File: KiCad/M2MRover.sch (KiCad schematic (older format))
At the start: 11 parts, among them J1 Light Detection, J10 MPU6050 Gyro & Acc GY-521, J2 Serial (Bluetooth), J3 Servo, J4 H-Bridge, J5 Ultrasonic Down, J6 Ultrasonic Forward, J7 Compass GY-273, J8 Left Hall, J9 Right Hall

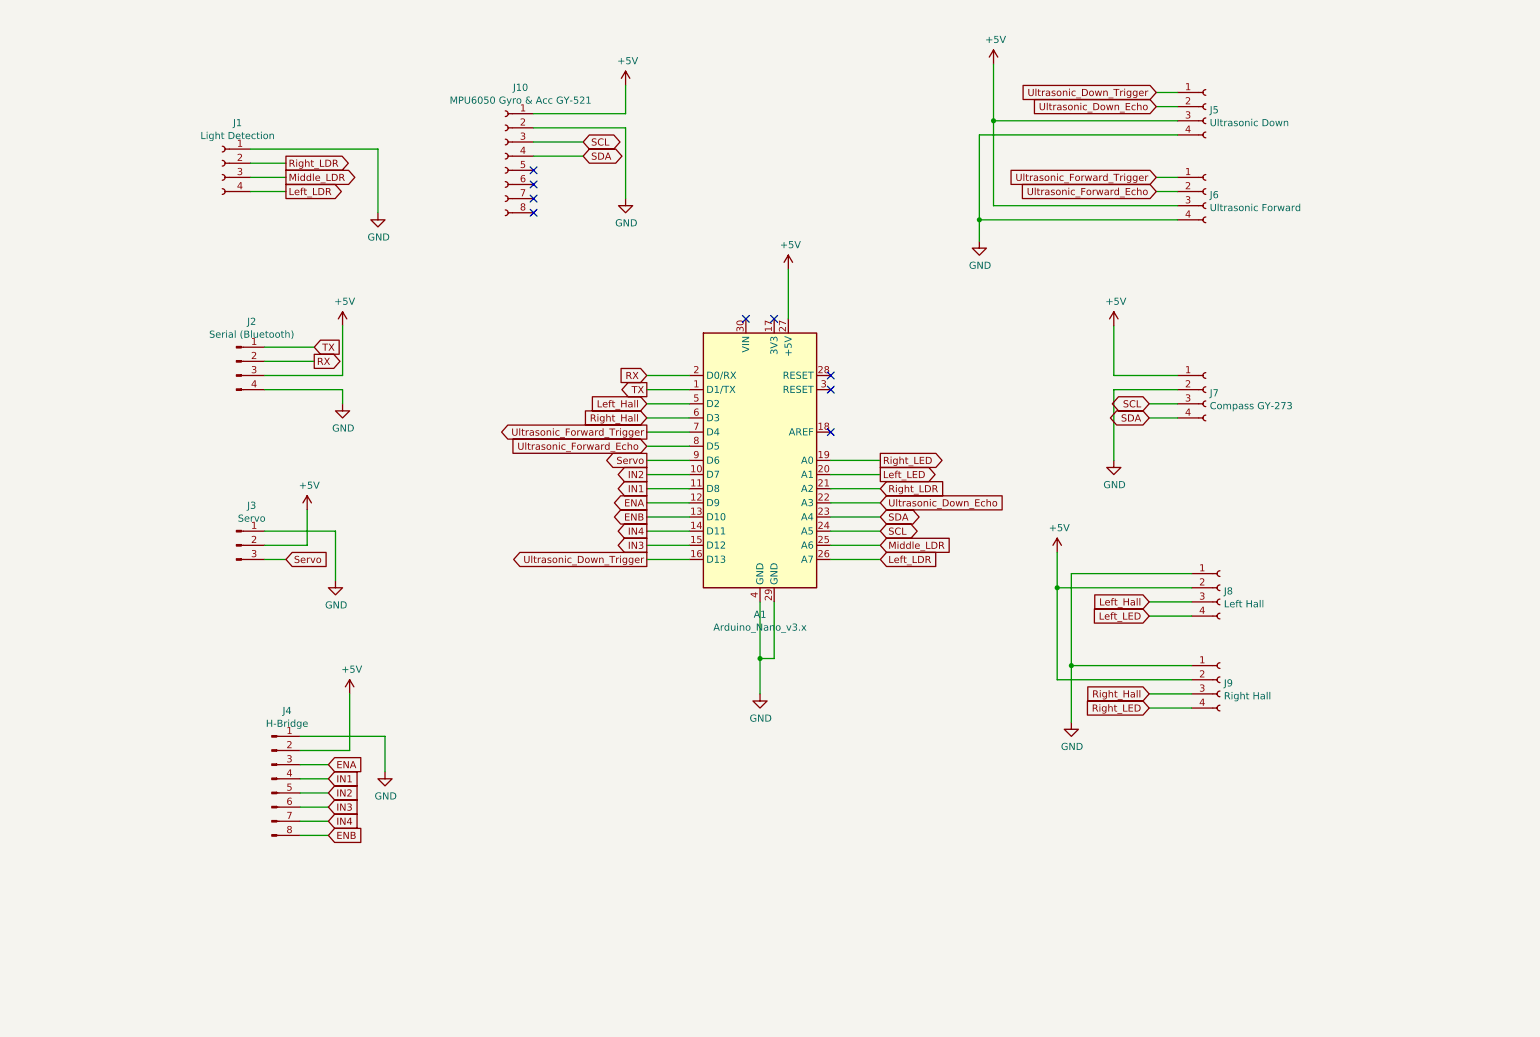
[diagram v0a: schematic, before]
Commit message: Add micro:bit connector
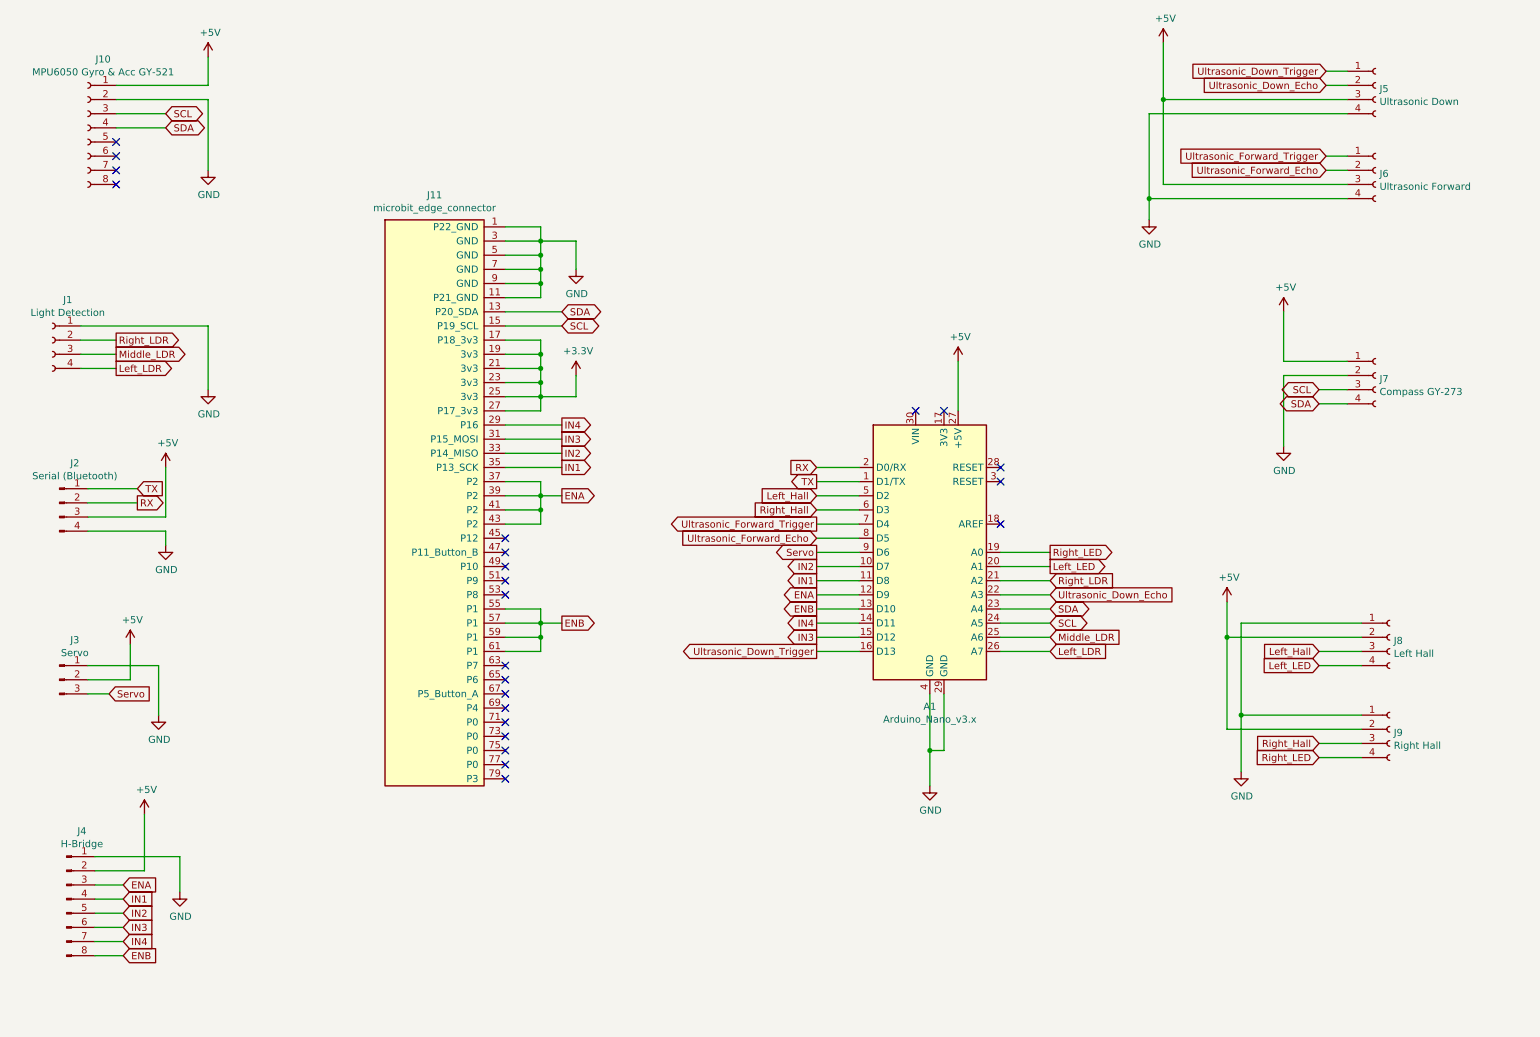
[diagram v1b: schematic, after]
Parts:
- added J11: microbit_edge_connector, MCU_Module_Microbit:4UCON_17909_02x401.27mm_Vertical, symbol MCU_Module_Microbit:microbit_edge_connector
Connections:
- net ENA: now also J11.37 (P2), J11.39 (P2), J11.41 (P2), J11.43 (P2)
- net ENB: now also J11.55 (P1), J11.57 (P1), J11.59 (P1), J11.61 (P1)
- net GND: now also J11.1 (P22_GND), J11.11 (P21_GND), J11.3 (GND), J11.5 (GND), J11.7 (GND), J11.9 (GND)
- net IN1: now also J11.35 (P13_SCK)
- net IN2: now also J11.33 (P14_MISO)
- net IN3: now also J11.31 (P15_MOSI)
- net IN4: now also J11.29 (P16)
- net SCL: now also J11.15 (P19_SCL)
- net SDA: now also J11.13 (P20_SDA)
- new net +3V3: J11.17 (P18_3v3), J11.19 (3v3), J11.21 (3v3), J11.23 (3v3), J11.25 (3v3), J11.27 (P17_3v3)
- no-connect marks 9 -> 23
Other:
- moved on the sheet: A1, J1, J10, J2, J3, J4, J5, J6, J7, J8, J9

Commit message: Add pull up resistors to LDRs and Hall effects
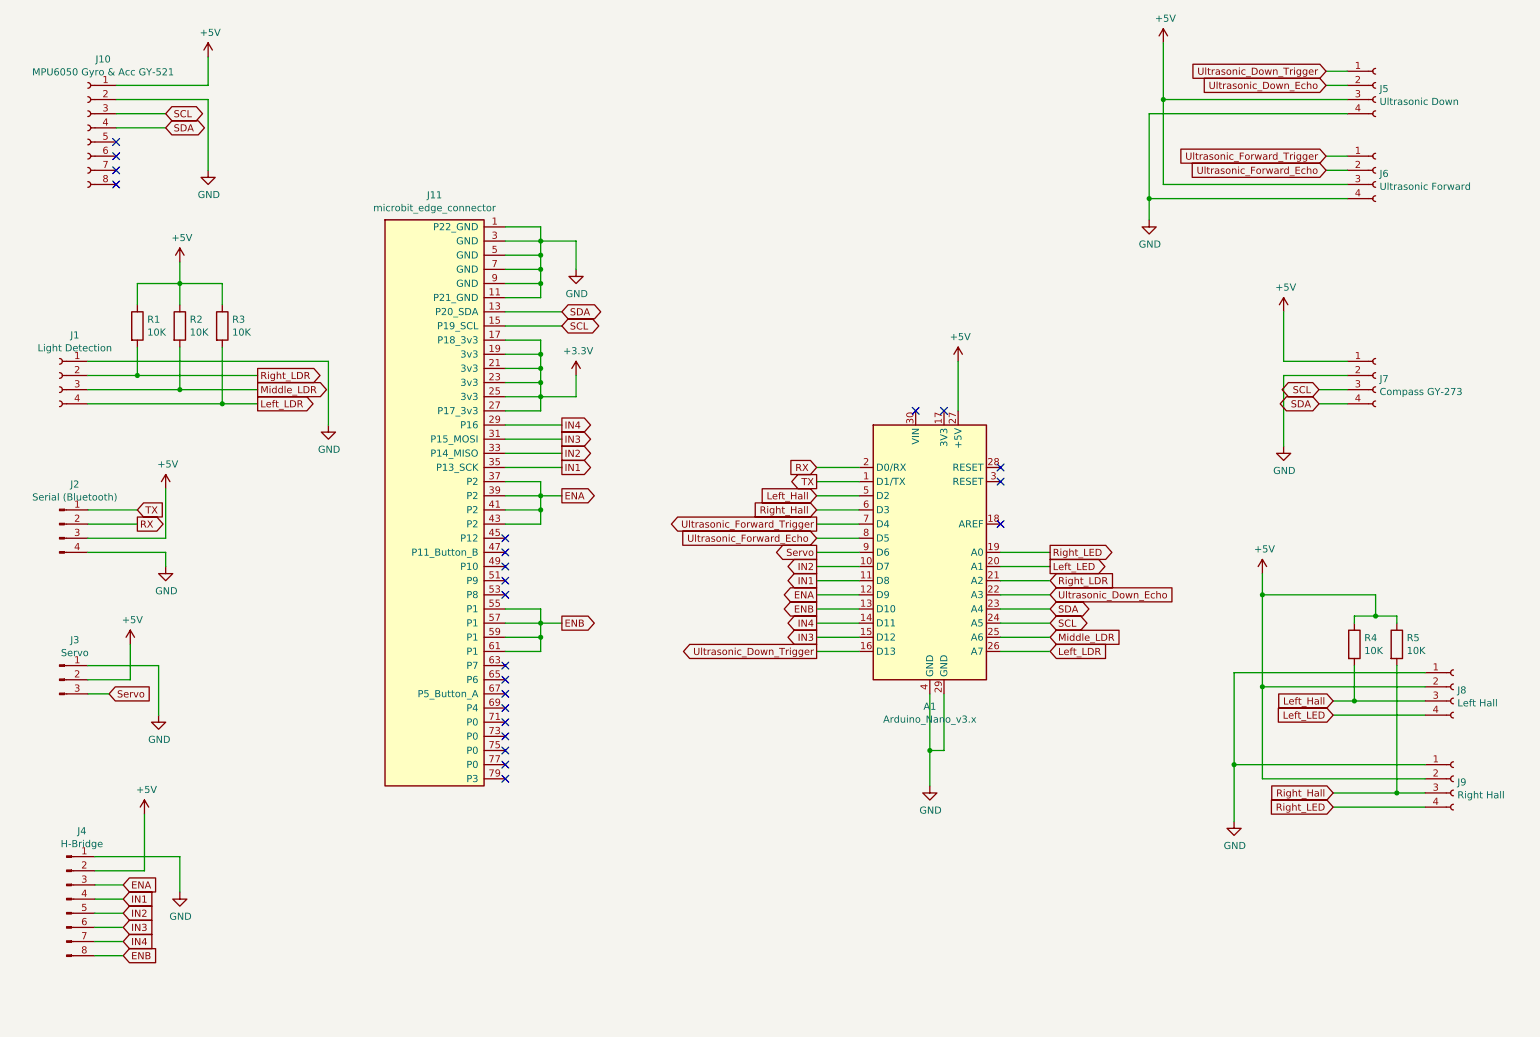
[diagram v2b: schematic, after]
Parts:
- added R1, R2, R3, R4, R5: 10K, symbol Device:R
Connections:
- net +5V: now also R1.1, R2.1, R3.1, R4.1, R5.1
- net Left_Hall: now also R4.2
- net Left_LDR: now also R3.2
- net Middle_LDR: now also R2.2
- net Right_Hall: now also R5.2
- net Right_LDR: now also R1.2
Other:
- moved on the sheet: J1, J2, J8, J9

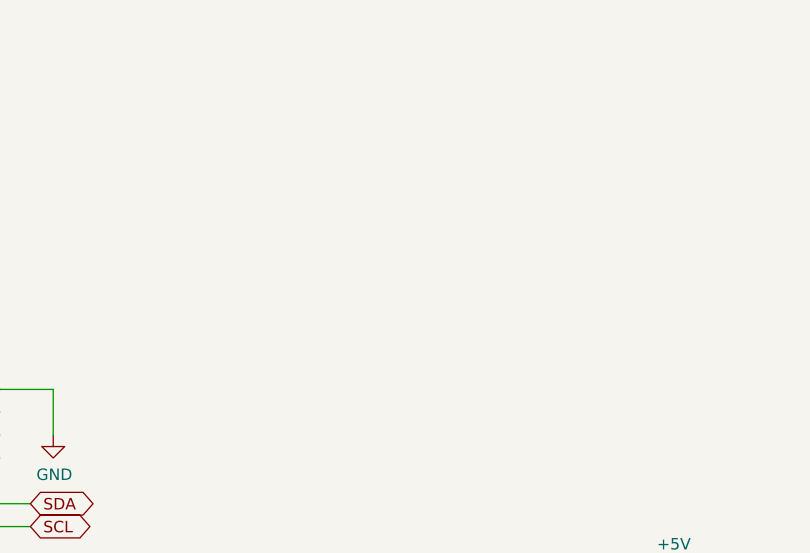
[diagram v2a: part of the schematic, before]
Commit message: Add 3.3V linear regulator for micro:bit power
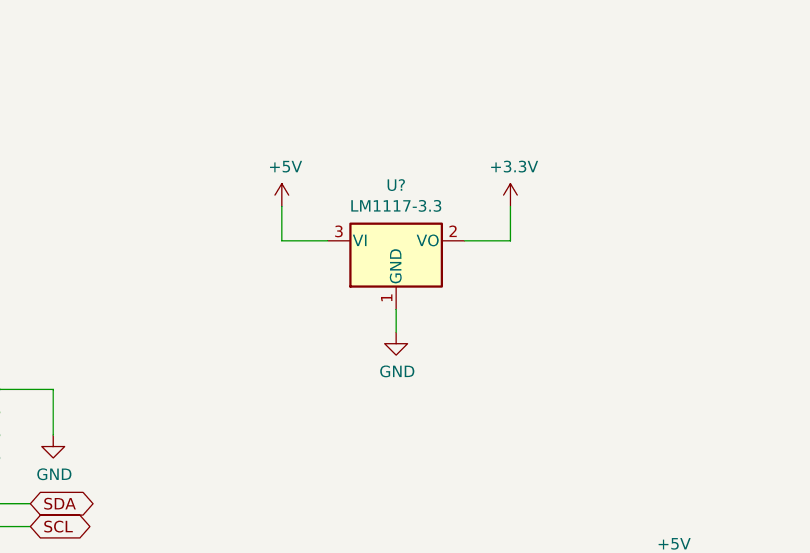
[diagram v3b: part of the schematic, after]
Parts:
- added U?: LM1117-3.3, Package_TO_SOT_THT:TO-220-3_Vertical, symbol Regulator_Linear:LM1117-3.3
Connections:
- net +3V3: now also U?.2 (VO)
- net +5V: now also U?.3 (VI)
- net GND: now also U?.1 (GND)
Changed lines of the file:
@@
 Wire Wire Line
 	9150 5250 9150 5900
+$Comp
+L Regulator_Linear:LM1117-3.3 U?
+U 1 1 5D5D0567
+P 6000 1550
+F 0 "U?" H 6000 1792 50  0000 C CNN
+F 1 "LM1117-3.3" H 6000 1701 50  0000 C CNN
+F 2 "Package_TO_SOT_THT:TO-220-3_Vertical" H 6000 1550 50  0001 C CNN
+F 3 "http://www.ti.com/lit/ds/symlink/lm1117.pdf" H 6000 1550 50  0001 C CNN
+	1    6000 1550
+	1    0    0    -1
+$EndComp
+$Comp
+L power:+5V #PWR?
+U 1 1 5D5DDFD0
+P 5500 1400
+F 0 "#PWR?" H 5500 1250 50  0001 C CNN
+F 1 "+5V" H 5515 1573 50  0000 C CNN
+F 2 "" H 5500 1400 50  0001 C CNN
+F 3 "" H 5500 1400 50  0001 C CNN
+	1    5500 1400
+	1    0    0    -1
+$EndComp
+$Comp
+L power:+3.3V #PWR?
+U 1 1 5D5DE8F7
+P 6500 1400
+F 0 "#PWR?" H 6500 1250 50  0001 C CNN
+F 1 "+3.3V" H 6515 1573 50  0000 C CNN
+F 2 "" H 6500 1400 50  0001 C CNN
+F 3 "" H 6500 1400 50  0001 C CNN
+	1    6500 1400
+	1    0    0    -1
+$EndComp
+$Comp
+L power:GND #PWR?
+U 1 1 5D5DF372
+P 6000 1950
+F 0 "#PWR?" H 6000 1700 50  0001 C CNN
+F 1 "GND" H 6005 1777 50  0000 C CNN
+F 2 "" H 6000 1950 50  0001 C CNN
+F 3 "" H 6000 1950 50  0001 C CNN
+	1    6000 1950
+	1    0    0    -1
+$EndComp
+Wire Wire Line
+	5500 1400 5500 1550
+Wire Wire Line
+	5500 1550 5700 1550
+Wire Wire Line
+	6300 1550 6500 1550
+Wire Wire Line
+	6500 1550 6500 1400
+Wire Wire Line
+	6000 1850 6000 1950
 $EndSCHEMATC

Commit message: Change micro:bit to h-bridge pin mapping
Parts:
- gave numbers to parts that had none: 1
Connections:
- net ENA: now also J11.55 (P1), J11.57 (P1), J11.59 (P1), J11.61 (P1); no longer J11.37 (P2), J11.39 (P2), J11.41 (P2), J11.43 (P2)
- net ENB: now also J11.37 (P2), J11.39 (P2), J11.41 (P2), J11.43 (P2); no longer J11.55 (P1), J11.57 (P1), J11.59 (P1), J11.61 (P1)
- net IN1: now also J11.33 (P14_MISO); no longer J11.35 (P13_SCK)
- net IN2: now also J11.35 (P13_SCK); no longer J11.33 (P14_MISO)
- net IN3: now also J11.29 (P16); no longer J11.31 (P15_MOSI)
- net IN4: now also J11.53 (P8); no longer J11.29 (P16)
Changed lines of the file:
@@
 Wire Wire Line
 	4500 3300 4250 3300
+Text GLabel 4400 3700 2    50   Output ~ 0
+IN1
 Text GLabel 4400 3800 2    50   Output ~ 0
-IN1
-Text GLabel 4400 3700 2    50   Output ~ 0
 IN2
-Text GLabel 4400 3600 2    50   Output ~ 0
+Text GLabel 4400 3500 2    50   Output ~ 0
 IN3
-Text GLabel 4400 3500 2    50   Output ~ 0
+Text GLabel 4400 4700 2    50   Output ~ 0
 IN4
+Text GLabel 4400 4900 2    50   Output ~ 0
+ENA
 Text GLabel 4400 4000 2    50   Output ~ 0
-ENA
-Text GLabel 4400 4900 2    50   Output ~ 0
 ENB
-Wire Wire Line
-	4250 4900 4400 4900
-Wire Wire Line
-	4250 4000 4400 4000
-Wire Wire Line
-	4000 3800 4400 3800
-Wire Wire Line
-	4000 3700 4400 3700
-Wire Wire Line
-	4000 3600 4400 3600
-Wire Wire Line
-	4000 3500 4400 3500
 NoConn ~ 4000 4300
 NoConn ~ 4000 4400
 NoConn ~ 4000 4500
 NoConn ~ 4000 4600
-NoConn ~ 4000 4700
 NoConn ~ 4000 5200
 NoConn ~ 4000 5300
@@
 	9150 5250 9150 5900
 $Comp
-L Regulator_Linear:LM1117-3.3 U?
+L Regulator_Linear:LM1117-3.3 U1
 U 1 1 5D5D0567
 P 6000 1550
-F 0 "U?" H 6000 1792 50  0000 C CNN
+F 0 "U1" H 6000 1792 50  0000 C CNN
 F 1 "LM1117-3.3" H 6000 1701 50  0000 C CNN
 F 2 "Package_TO_SOT_THT:TO-220-3_Vertical" H 6000 1550 50  0001 C CNN
@@
 $EndComp
 $Comp
-L power:+5V #PWR?
+L power:+5V #PWR06
 U 1 1 5D5DDFD0
 P 5500 1400
-F 0 "#PWR?" H 5500 1250 50  0001 C CNN
+F 0 "#PWR06" H 5500 1250 50  0001 C CNN
 F 1 "+5V" H 5515 1573 50  0000 C CNN
 F 2 "" H 5500 1400 50  0001 C CNN
@@
 $EndComp
 $Comp
-L power:+3.3V #PWR?
+L power:+3.3V #PWR08
 U 1 1 5D5DE8F7
 P 6500 1400
-F 0 "#PWR?" H 6500 1250 50  0001 C CNN
+F 0 "#PWR08" H 6500 1250 50  0001 C CNN
 F 1 "+3.3V" H 6515 1573 50  0000 C CNN
 F 2 "" H 6500 1400 50  0001 C CNN
@@
 $EndComp
 $Comp
-L power:GND #PWR?
+L power:GND #PWR07
 U 1 1 5D5DF372
 P 6000 1950
-F 0 "#PWR?" H 6000 1700 50  0001 C CNN
+F 0 "#PWR07" H 6000 1700 50  0001 C CNN
 F 1 "GND" H 6005 1777 50  0000 C CNN
 F 2 "" H 6000 1950 50  0001 C CNN
@@
 Wire Wire Line
 	6000 1850 6000 1950
+Wire Wire Line
+	4000 3500 4400 3500
+Wire Wire Line
+	4000 3700 4400 3700
+Wire Wire Line
+	4000 3800 4400 3800
+Wire Wire Line
+	4250 4000 4400 4000
+Wire Wire Line
+	4000 4700 4400 4700
+Wire Wire Line
+	4250 4900 4400 4900
+NoConn ~ 4000 3600
 $EndSCHEMATC

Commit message: Add PWR_FLG to GND to fix ERC errors
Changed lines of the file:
@@
 	4250 4900 4400 4900
 NoConn ~ 4000 3600
+$Comp
+L power:PWR_FLAG #FLG0101
+U 1 1 5D5DC827
+P 1700 6500
+F 0 "#FLG0101" H 1700 6575 50  0001 C CNN
+F 1 "PWR_FLAG" H 1700 6673 50  0000 C CNN
+F 2 "" H 1700 6500 50  0001 C CNN
+F 3 "~" H 1700 6500 50  0001 C CNN
+	1    1700 6500
+	1    0    0    -1
+$EndComp
+Connection ~ 1700 6550
+Wire Wire Line
+	1700 6550 1700 6500
 $EndSCHEMATC

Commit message: Add mounting holes
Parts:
- added H1, H2, H3, H4: MountingHole, MountingHole:MountingHole_4.3mm_M4_Pad, symbol Mechanical:MountingHole
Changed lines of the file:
@@
 Wire Wire Line
 	1700 6550 1700 6500
+$Comp
+L Mechanical:MountingHole H1
+U 1 1 5D604FCC
+P 3350 7050
+F 0 "H1" H 3450 7096 50  0000 L CNN
+F 1 "MountingHole" H 3450 7005 50  0000 L CNN
+F 2 "MountingHole:MountingHole_4.3mm_M4_Pad" H 3350 7050 50  0001 C CNN
+F 3 "~" H 3350 7050 50  0001 C CNN
+	1    3350 7050
+	1    0    0    -1
+$EndComp
+$Comp
+L Mechanical:MountingHole H2
+U 1 1 5D605AC0
+P 3350 7250
+F 0 "H2" H 3450 7296 50  0000 L CNN
+F 1 "MountingHole" H 3450 7205 50  0000 L CNN
+F 2 "MountingHole:MountingHole_4.3mm_M4_Pad" H 3350 7250 50  0001 C CNN
+F 3 "~" H 3350 7250 50  0001 C CNN
+	1    3350 7250
+	1    0    0    -1
+$EndComp
+$Comp
+L Mechanical:MountingHole H3
+U 1 1 5D606344
+P 3350 7450
+F 0 "H3" H 3450 7496 50  0000 L CNN
+F 1 "MountingHole" H 3450 7405 50  0000 L CNN
+F 2 "MountingHole:MountingHole_4.3mm_M4_Pad" H 3350 7450 50  0001 C CNN
+F 3 "~" H 3350 7450 50  0001 C CNN
+	1    3350 7450
+	1    0    0    -1
+$EndComp
+$Comp
+L Mechanical:MountingHole H4
+U 1 1 5D606BD0
+P 3350 7650
+F 0 "H4" H 3450 7696 50  0000 L CNN
+F 1 "MountingHole" H 3450 7605 50  0000 L CNN
+F 2 "MountingHole:MountingHole_4.3mm_M4_Pad" H 3350 7650 50  0001 C CNN
+F 3 "~" H 3350 7650 50  0001 C CNN
+	1    3350 7650
+	1    0    0    -1
+$EndComp
 $EndSCHEMATC
